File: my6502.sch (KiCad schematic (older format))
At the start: 23 parts

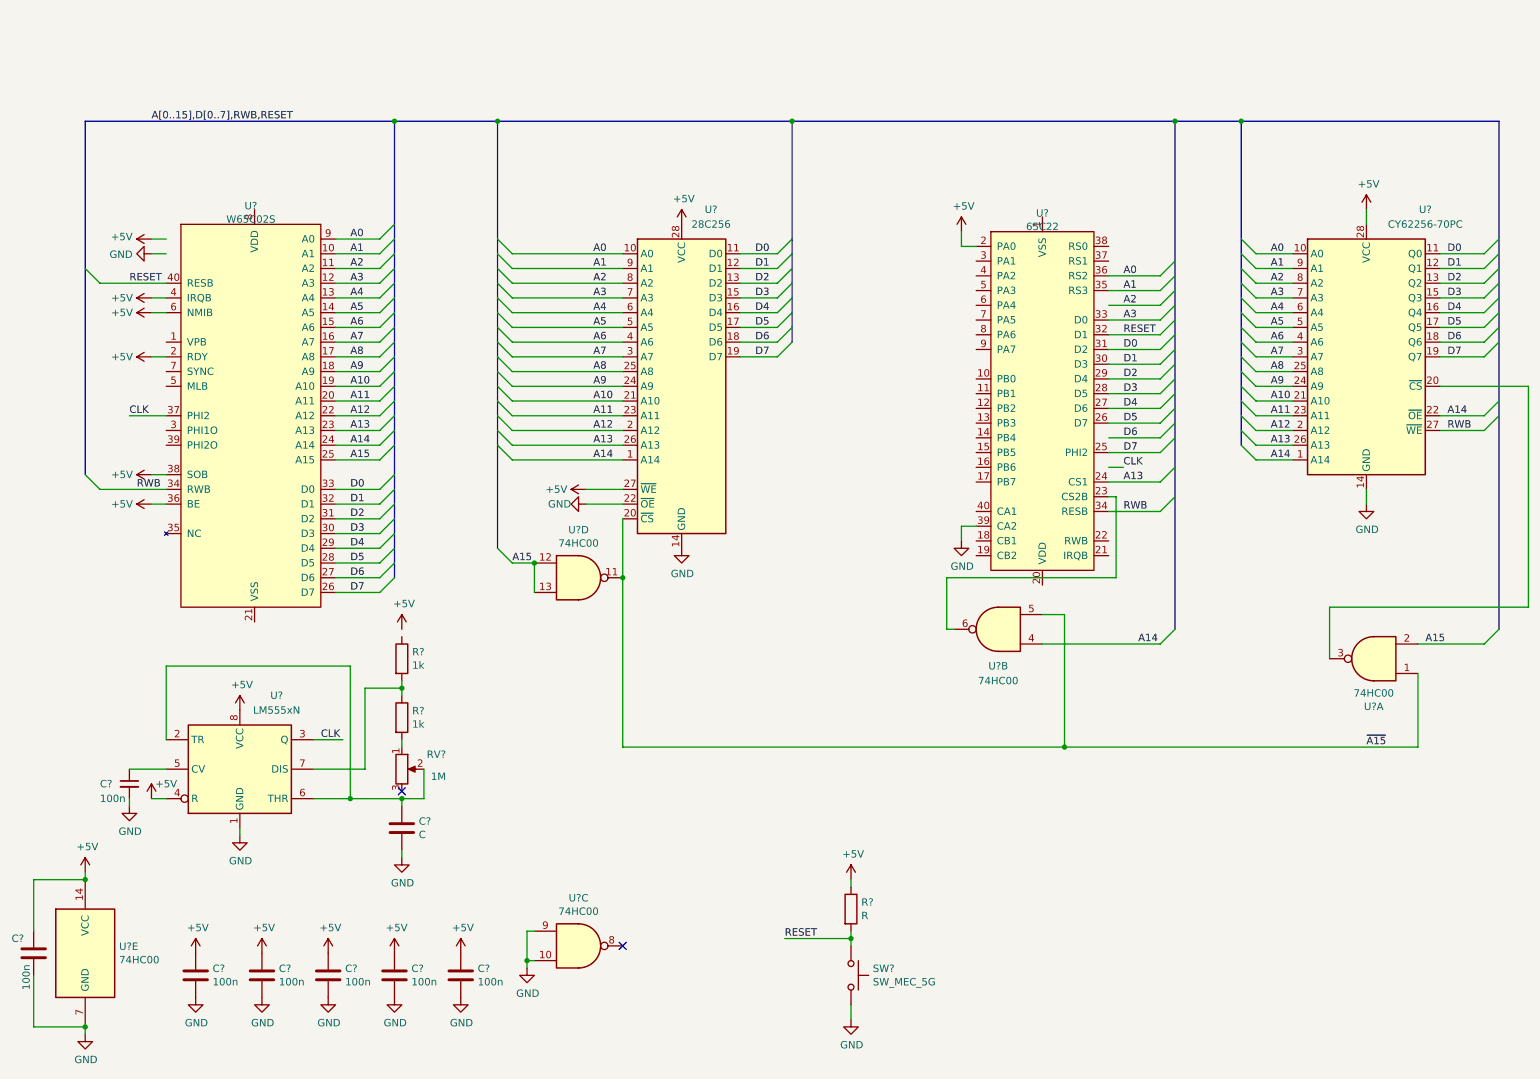
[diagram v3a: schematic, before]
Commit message: Add manual clock pulse button (incomplete)
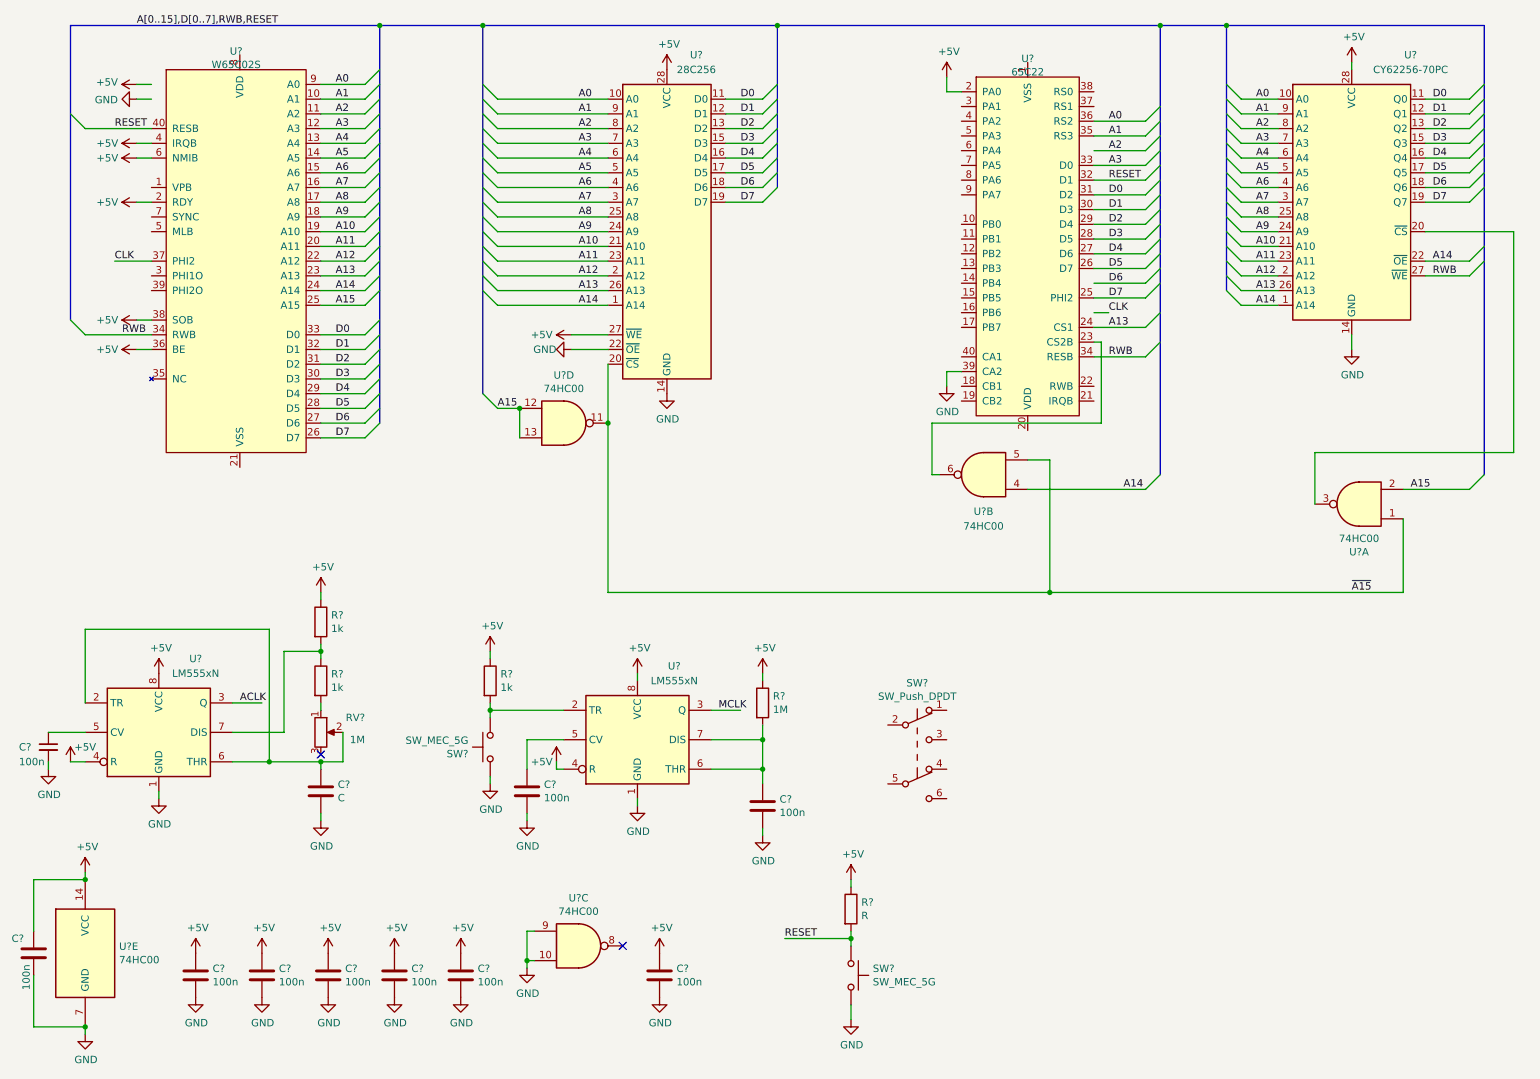
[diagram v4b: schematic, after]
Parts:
- added C? (x3): 100n, symbol Device:C
- added R?: 1M, symbol Device:R
- added R?: 1k, symbol Device:R
- added SW?: SW_Push_DPDT, symbol Switch:SW_Push_DPDT
- added SW?: SW_MEC_5G, symbol Switch:SW_MEC_5G
- added U?: LM555xN, Package_DIP:DIP-8_W7.62mm, symbol Timer:LM555xN
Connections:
- net labels added: ACLK, MCLK
- wire segments 161 -> 182
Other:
- moved on the sheet: C?, R?, RV?, U?, U?A, U?B, U?D

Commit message: Incomplete work on primarily display and keys
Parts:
- added RV?: 1M, symbol Device:R_POT
- added SW? (x6): SW_Push, symbol Switch:SW_Push
- added U8: HD44780, symbol 6502:HD44780
- gave numbers to parts that had none: 27
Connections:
- net labels added: CA1, CA2, CB1, CB2, PA0, PA1, PA2, PA3, PA4, PA5, PA6, PA7, PB0, PB1, PB2, PB3, PB4, PB5, PB6, PB7
- wire segments 182 -> 247
- no-connect marks 2 -> 3
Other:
- note added: "Astable oscillator"
- note added: "Clock Module"
- note added: "Decoupling Capacitors"
- note added: "Monostable oscillator"
- moved on the sheet: C1, C10, C11, C2, C3, C4, C5, C6, C7, C8, C9, R1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

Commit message: Uncomitted changes
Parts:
- added C12: 100n, symbol Device:C
- added R6: 1k, symbol Device:R
- added RV?: 10k?, symbol Device:R_POT
- added U?: 74HC00, symbol 74xx:74HC00
- R5: value R -> 1k
- RV2: renamed from RV?; value 1M -> 10k?
- gave numbers to parts that had none: 6
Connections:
- net +5V: now also U3.8 (VDD), R6.2; no longer U3.2 (RDY), U3.4 (IRQB)
- net A12: now also U1.2
- net A13: now also U1.5
- net A14: now also U1.4; no longer U7.22 (~OE)
- net A15: no longer U1.2
- net GND: now also U3.21 (VSS), C12.2, RV?.1; no longer U1.10, U1.9, U5.22 (~OE)
- net PA5: now also U8.4 (RS)
- net PA6: now also U8.5 (RW)
- net PA7: now also U8.6 (E)
- net RESET: now also C12.1; no longer U6.34 (RESB)
- net ~A15: now also U5.22 (~OE), U6.24 (CS1), U?.1; no longer U1.1, U1.5
- net at U7.20 (~CS): now also U7.22 (~OE), U?.3; no longer U1.3
- net at U8.3 (VEE): now also RV?.2
- net at U1.6: now also U1.10, U1.9
- net IRQB: now reaches U6.21 (IRQB)
- net IRQB: now also U3.4 (IRQB)
- net at U6.23 (CS2B): now also U1.3, U?.2
- net at U1.8: now also U1.1
- new net: R6.1, U3.2 (RDY)
- no-connect marks 3 -> 8
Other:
- note added: "32k EEPROM"
- note added: "32k SRAM"
- note added: "65C02 Microprocessor"
- note added: "65C22 Versatile Interface Adapter (VIA)"
- note added: "TODO:\n\nHandle unused logic gates"
- moved on the sheet: R5, RV2, SW2, SW4, SW5, SW6, SW7, SW8, SW9, U1A, U1B, U1C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

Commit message: Updates to the clock module
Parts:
- added C? (x3): 100n, symbol Device:C
- added D? (x3): LED, symbol Device:LED
- added JP? (x3): Jumper_2_Open, symbol Jumper:Jumper_2_Open
- added JP?: Jumper_3_Open, symbol Jumper:Jumper_3_Open
- added R? (x2): 1k, symbol Device:R
- added R? (x3): 220, symbol Device:R
- added U?: LM555xN, Package_DIP:DIP-8_W7.62mm, symbol Timer:LM555xN
- added U? (x8): 74HC00, symbol 74xx:74HC00
- added X?: CXO_DIP14, Oscillator:Oscillator_DIP-14, symbol Oscillator:CXO_DIP14
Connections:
- net +5V: now also C?.1, C?.1, R?.1, R?.1, U?.8 (VCC), X?.14 (Vcc)
- net ACLK: now also JP?.1 (A), U?.1
- net CLK: now also JP?.1 (A), U?.3
- net GND: now also SW3.5 (B), C?.2, C?.2, C?.2, D?.1 (K), D?.1 (K), D?.1 (K), U?.1, U?.1 (GND), U?.2, U?.6 (THR), X?.7 (GND)
- net MCLK: now also JP?.1 (A), U?.2
- net at SW3.4 (A): now also R?.2, U?.4 (R)
- net at SW3.6 (C): now also R?.2, U?.2 (TR)
- new net: C?.1, U?.5 (CV)
- new net: D?.2 (A), R?.1 (x3)
- new net: JP?.2 (B), R?.2 (x3)
- new net: U?.1, U?.3 (x2)
- new net: U?.2, U?.3 (x2)
- new net: JP?.1 (A), U?.3
- new net: JP?.2 (C), U?.1
- new net: U?.1, U?.2, U?.3
- new net: JP?.3 (B), X?.8 (OUT)
- new net CLKSEL: U?.1, U?.2, U?.2, U?.3 (Q)
- new net HLT: U?.1, U?.2
- no-connect marks 8 -> 10
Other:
- note added: "Astable/monostable selector with debounce"
- note added: "FIXME: Pins of clock osc\nseems to be wrong"
- note added: "FIXME: no decoupling caps for 74HC00 <——\n\n"
- note added: "Make sure switch is\nbreak-before-make"
- moved on the sheet: C11, C12, C2, C5, C9, R1, R2, R3, R4, R5, R6, RV1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

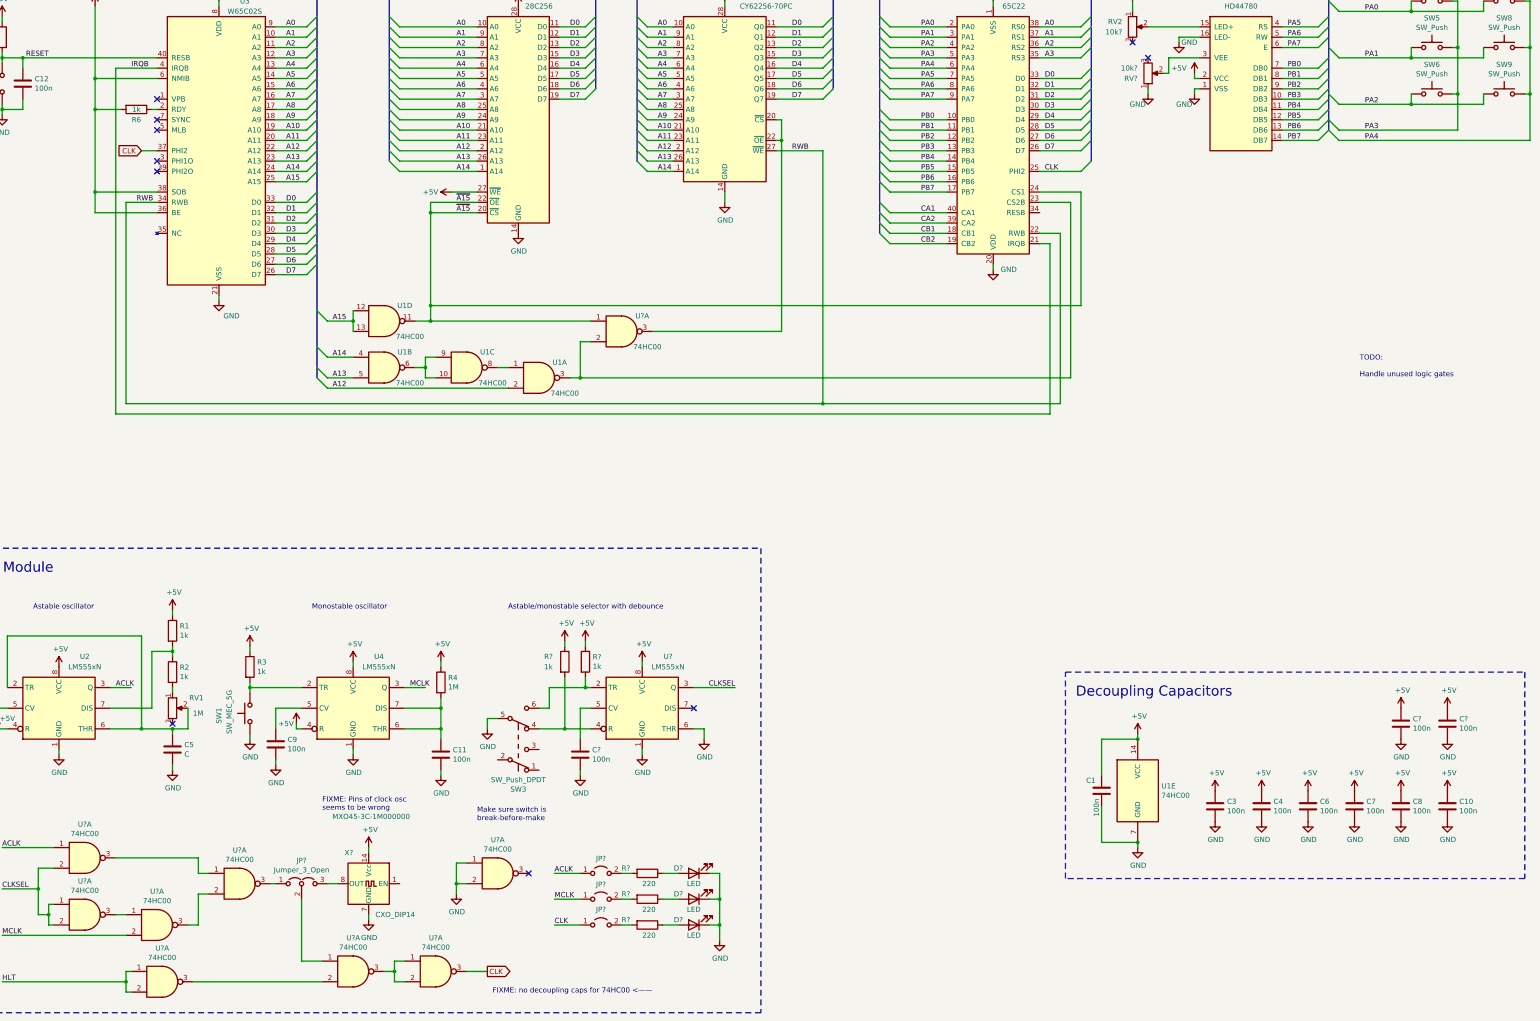
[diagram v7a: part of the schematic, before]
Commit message: Pick footprints for a many components
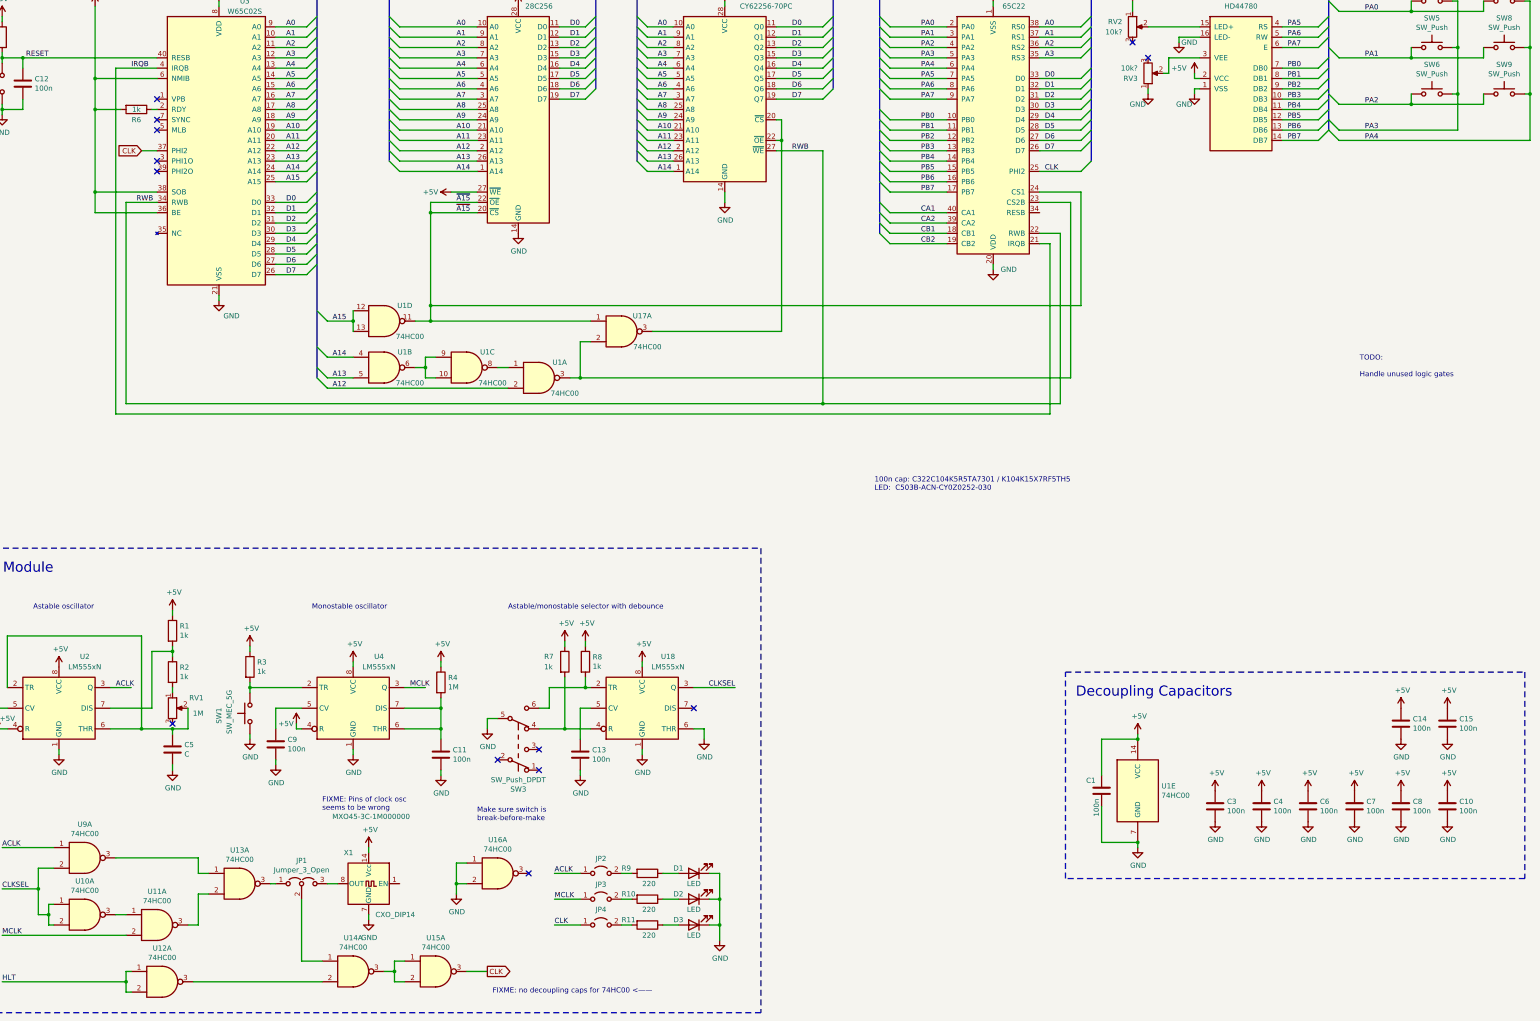
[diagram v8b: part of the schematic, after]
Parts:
- C1, C10, C11, C12, C2, C3, C4, C6, C7, C8, C9: footprint (none) -> Capacitor_THT:C_Disc_D5.1mm_W3.2mm_P5.00mm
- C13, C14, C15: renamed from C?; footprint (none) -> Capacitor_THT:C_Disc_D5.1mm_W3.2mm_P5.00mm
- D1, D2, D3: renamed from D?; footprint (none) -> LED_THT:LED_D5.0mm
- R1, R2, R3, R4, R5, R6, RV1, RV2: footprint (none) -> Resistor_THT:R_Axial_DIN0207_L6.3mm_D2.5mm_P7.62mm_Horizontal
- R10, R11, R7, R8, R9: renamed from R?; footprint (none) -> Resistor_THT:R_Axial_DIN0207_L6.3mm_D2.5mm_P7.62mm_Horizontal
- RV3: renamed from RV?; footprint (none) -> Resistor_THT:R_Axial_DIN0207_L6.3mm_D2.5mm_P7.62mm_Horizontal
- U1: footprint (none) -> Package_DIP:DIP-14_W7.62mm_LongPads
- U10, U11, U12, U13, U14, U15, U16, U17, U9: renamed from U?; footprint (none) -> Package_DIP:DIP-14_W7.62mm_LongPads
- U3, U6: footprint (none) -> Package_DIP:DIP-40_W15.24mm_Socket_LongPads
- U5: footprint (none) -> Package_DIP:DIP-28_W15.24mm_Socket_LongPads
- gave numbers to parts that had none: 6
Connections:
- no-connect marks 10 -> 13
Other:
- note added: "100n cap: C322C104K5R5TA7301 / K104K15X7RF5TH5\nLED: C503B-ACN-CY0Z0252-030"
